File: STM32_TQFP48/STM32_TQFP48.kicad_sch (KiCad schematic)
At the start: 79 parts, among them SW1 SW_Push, SW2 SW_Push, U1 STM32L010C6Tx, Y1 Crystal

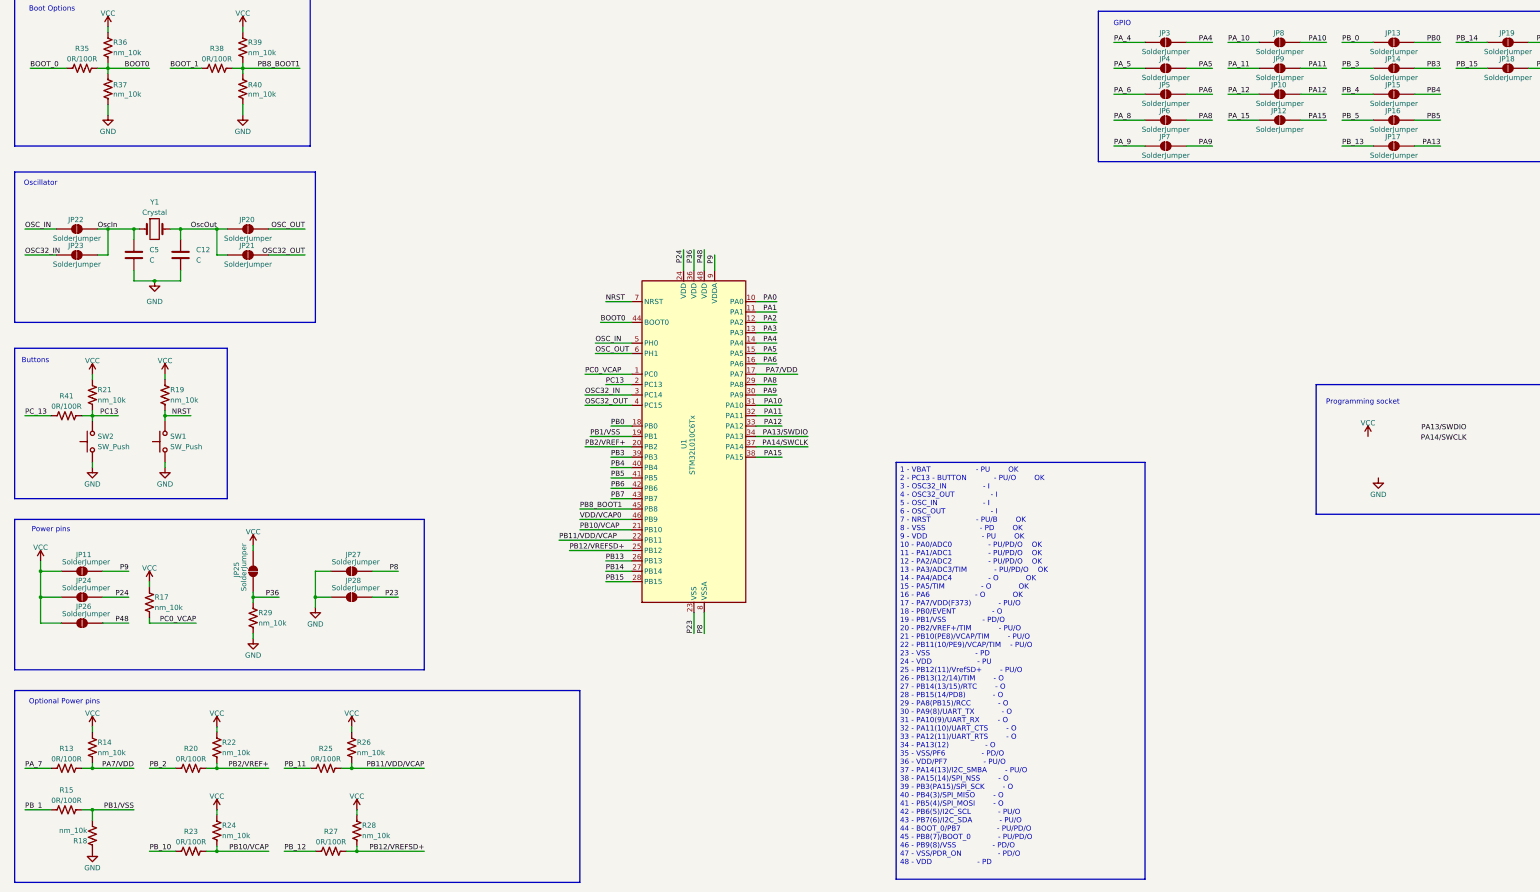
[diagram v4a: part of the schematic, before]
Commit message: STM32_TQFP48: Uzupełnienie Optional power pin, poprawa Power pin i dodanie złącza do programowania.
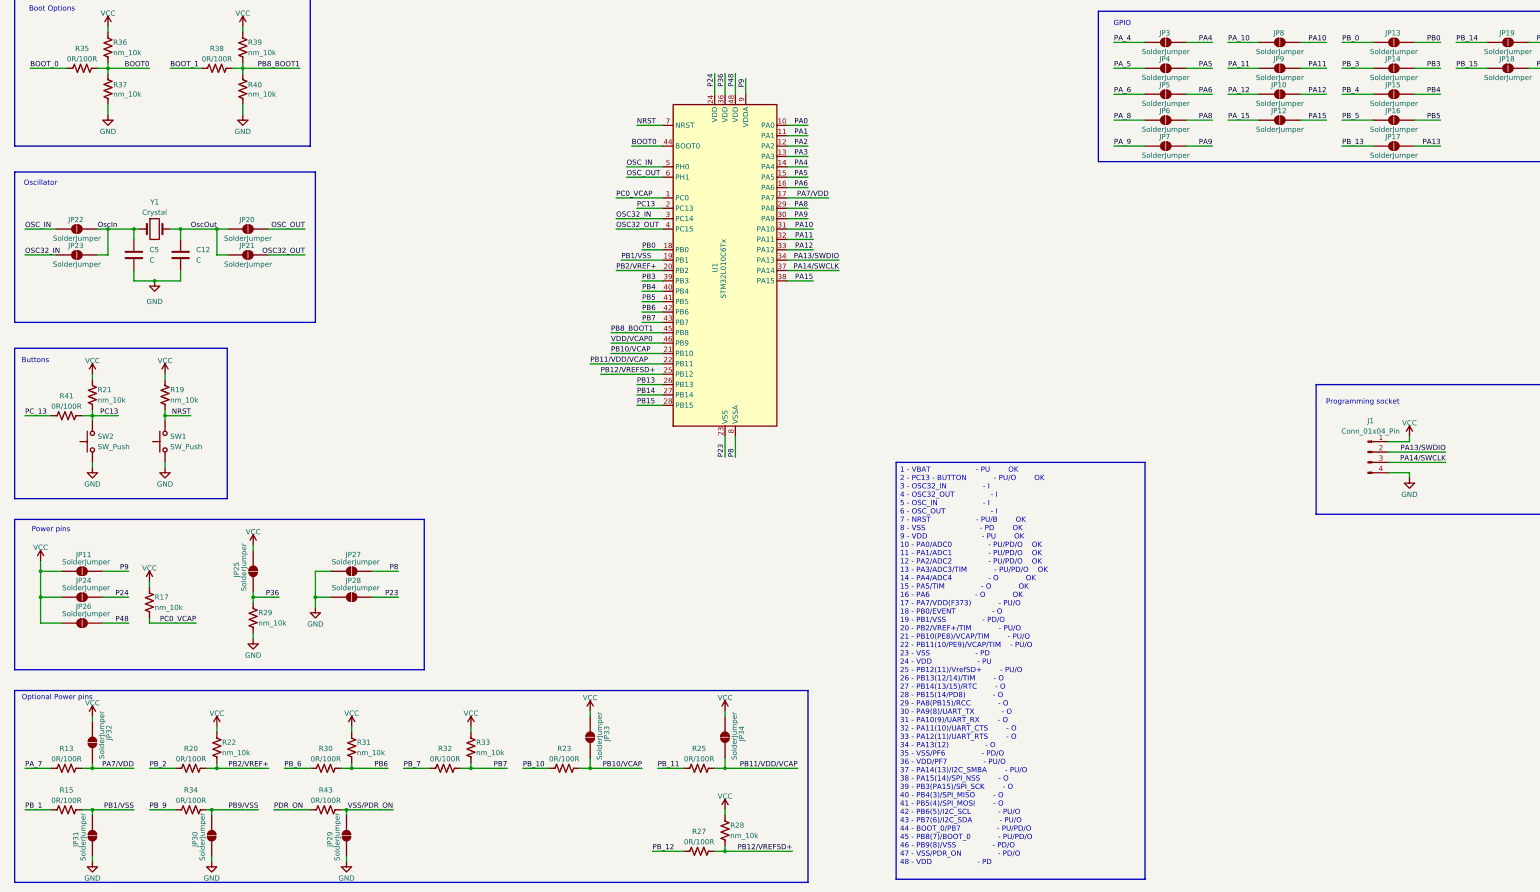
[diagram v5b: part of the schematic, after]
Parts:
- removed R14, R18, R24, R26: nm_10k, symbol Device:R_US
- added J1: Conn_01x04_Pin, symbol Connector:Conn_01x04_Pin
- added JP29, JP30, JP31, JP32, JP33, JP34: SolderJumper, symbol Jumper:SolderJumper_2_Open
- added R30, R32, R34, R43: 0R/100R, symbol Device:R_US
- added R31, R33: nm_10k, symbol Device:R_US
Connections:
- net GND: now also J1.4 (Pin_4), JP29.1 (A), JP30.1 (A), JP31.1 (A)
- net PA13/SWDIO: now also J1.2 (Pin_2)
- net PA14/SWCLK: now also J1.3 (Pin_3)
- net PA7/VDD: now also JP32.2 (B)
- net PB1/VSS: now also JP31.2 (B)
- net PB10/VCAP: now also JP33.2 (B)
- net PB11/VDD/VCAP: now also JP34.2 (B)
- net PB6: now also R30.2, R31.2
- net PB7: now also R32.2, R33.2
- net VCC: now also J1.1 (Pin_1), JP32.1 (A), JP33.1 (A), JP34.1 (A), R31.1, R33.1
- new net PB9/VSS: JP30.2 (B), R34.2
- new net PB_6: R30.1
- new net PB_7: R32.1
- new net PB_9: R34.1
- new net PDR_ON: R43.1
- new net VSS/PDR_ON: JP29.2 (B), R43.2
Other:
- moved on the sheet: R23, R25, R27, R28, U1

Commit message: STM32_TQFP48: Reset numeracji komponenów
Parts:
- renumbered C6 to C1, C2 to C10, C3 to C11, C4 to C12, C5 to C2, C7 to C3, C8 to C4, C12 to C5, C9 to C6, C10 to C7, C11 to C8, C1 to C9, JP22 to JP1, JP21 to JP10, JP25 to JP11, JP29 to JP12, JP27 to JP13, JP28 to JP14, JP33 to JP15, JP34 to JP16, JP3 to JP17, JP4 to JP18, JP5 to JP19, JP23 to JP2, JP6 to JP20, JP7 to JP21, JP8 to JP22, JP9 to JP23, JP10 to JP24, JP12 to JP25, JP13 to JP26, JP14 to JP27, JP15 to JP28, JP16 to JP29, JP11 to JP3, JP17 to JP30, JP19 to JP31, JP18 to JP32, JP24 to JP4, JP26 to JP5, JP32 to JP6, JP31 to JP7, JP30 to JP8, JP20 to JP9, R16 to R1, R19 to R10, R20 to R11, R34 to R12, R38 to R13, R22 to R14, R39 to R15, R40 to R16, R29 to R17, R30 to R18, R43 to R19, R41 to R2, R31 to R20, R32 to R21, R33 to R22, R25 to R24, R27 to R25, R28 to R26, R2 to R27, R1 to R28, R3 to R29, R13 to R3, R4 to R30, R5 to R31, R6 to R32, R7 to R33, R8 to R34, R9 to R35, R10 to R36, R11 to R37, R12 to R38, R15 to R4, R35 to R5, R21 to R6, R36 to R7, R37 to R8, R17 to R9, SW2 to SW1, SW1 to SW2

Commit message: STM32_TQFP48(.sch): Dodanie ukrytych pinów zasilania na schemacie STMa, dodanie goldpinów i przypisanie im wyprowadzeń
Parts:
- added J2, J3: Conn_01x19_Pin, symbol Connector:Conn_01x19_Pin
- added JP33: SolderJumper, symbol Jumper:SolderJumper_2_Open
- added R39: 0R/100R, symbol Device:R_US
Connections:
- net BOOT_0: now also J2.6 (Pin_6)
- net BOOT_1: now also J2.5 (Pin_5)
- net GND: now also J2.2 (Pin_2), J3.18 (Pin_18), JP33.1 (A)
- net P23: no longer U1.35 (VSS), U1.47 (VSS)
- net PA_0: now also J3.2 (Pin_2)
- net PA_1: now also J3.3 (Pin_3)
- net PA_10: now also J2.16 (Pin_16)
- net PA_11: now also J2.15 (Pin_15)
- net PA_12: now also J2.14 (Pin_14)
- net PA_15: now also J2.12 (Pin_12)
- net PA_2: now also J3.4 (Pin_4)
- net PA_3: now also J3.5 (Pin_5)
- net PA_4: now also J3.6 (Pin_6)
- net PA_5: now also J3.7 (Pin_7)
- net PA_6: now also J3.8 (Pin_8)
- net PA_7: now also J3.9 (Pin_9)
- net PA_8: now also J2.18 (Pin_18)
- net PA_9: now also J2.17 (Pin_17)
- net PB_0: now also J3.10 (Pin_10)
- net PB_1: now also J3.11 (Pin_11)
- net PB_10: now also J3.13 (Pin_13)
- net PB_11: now also J3.14 (Pin_14)
- net PB_12: now also J3.15 (Pin_15)
- net PB_13: now also J3.16 (Pin_16)
- net PB_14: now also J3.17 (Pin_17)
- net PB_15: now also J2.19 (Pin_19)
- net PB_2: now also J3.12 (Pin_12)
- net PB_3: now also J2.11 (Pin_11)
- net PB_4: now also J2.10 (Pin_10)
- net PB_5: now also J2.9 (Pin_9)
- net PB_6: now also J2.8 (Pin_8)
- net PB_7: now also J2.7 (Pin_7)
- net PB_9: now also J2.4 (Pin_4)
- net PC_13: now also J3.1 (Pin_1)
- net PDR_ON: now also J2.3 (Pin_3)
- net VCC: now also J2.1 (Pin_1), J3.19 (Pin_19)
- net VSS/PDR_ON: now also U1.47 (VSS)
- new net PF_1: J2.13 (Pin_13), R39.1
- new net PF_1/VSS: JP33.2 (B), R39.2, U1.35 (VSS)

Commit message: STM32_TQFP48(.sch): Zamiana zworek na rezystory dla kilku GPIO.
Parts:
- removed JP19, JP20, JP21: SolderJumper, symbol Jumper:SolderJumper_2_Open
- added R40, R41, R42: 0R/100R, symbol Device:R_US
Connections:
- net PA6: now also R40.2
- net PA8: now also R42.2
- net PA9: now also R41.1
- net PA_6: now also R40.1
- net PA_8: now also R42.1
- net PA_9: now also R41.2
- net PB11/VDD/VCAP: no longer JP16.2 (B), R24.2
- new net: JP16.2 (B), R24.2
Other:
- moved on the sheet: C10, C11, C12, C9, J1, J2, J3, JP17, JP18, JP22, JP23, JP24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
